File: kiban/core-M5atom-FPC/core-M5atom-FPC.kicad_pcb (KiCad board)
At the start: 2 copper layers, 49 x 40 mm, 18 parts, among them J12 TP_VIN, J13 TP_3V3, J14 TP_PGND, J15 TP_PGND, J16 ESP32-01, J17 ESP32-01, J18 TP_PGND, J3 M5atom-L, J4 M5atomS3-R, J5 3V3, J6 5V, J9 I2C, U1 AE-BNO055

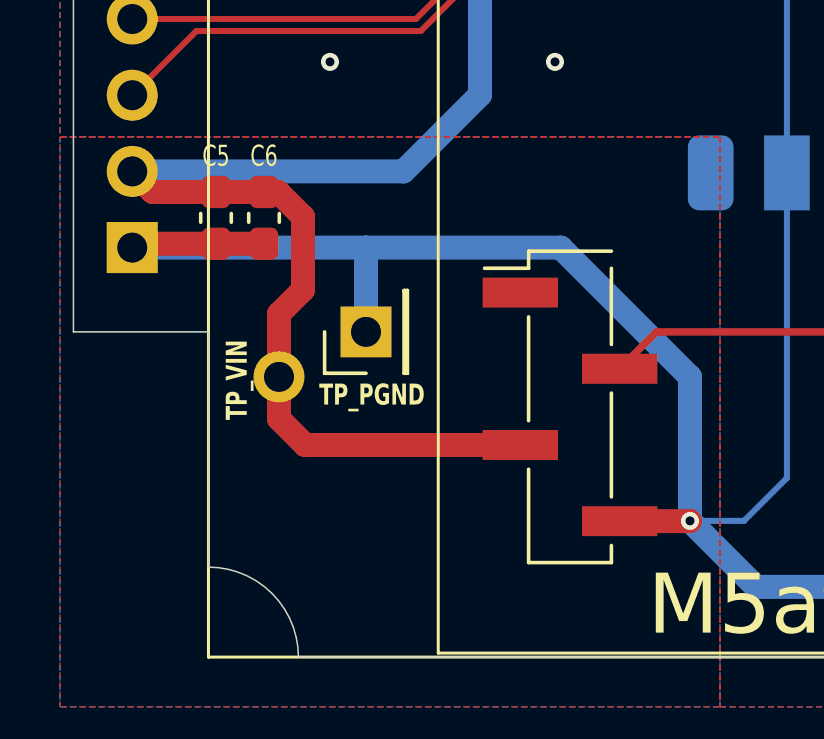
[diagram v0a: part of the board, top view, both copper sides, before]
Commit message: kiban: core-M5atom-FPC layout update + v02 iteration
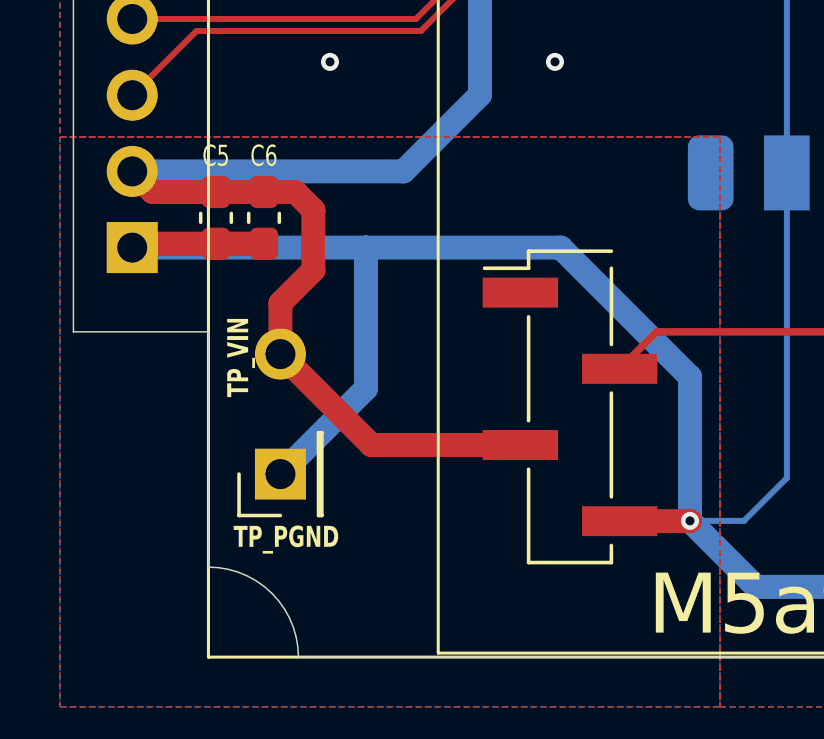
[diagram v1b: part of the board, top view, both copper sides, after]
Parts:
- moved J15 5.53 mm to (-17.6, 13.9)
- moved J12 0.76 mm to (-17.6, 9.90)
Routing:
- net GND: track 131.7 -> 137.6 mm
- net +5V: track 67.9 -> 67.2 mm
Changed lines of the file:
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@@
 	(footprint "Connector_PinHeader_2.54mm:PinHeader_1x01_P2.54mm_Vertical"
 		(layer "F.Cu")
-		(at -14.747867 9.1587 90)
+		(at -17.6 13.9 90)
 		(descr "Through hole straight pin header, 1x01, 2.54mm pitch, single row")
 		(tags "Through hole pin header THT 1x01 2.54mm single row")
@@
 	(footprint "Connector_PinHeader_2.54mm:PinHeader_1x01_P2.54mm_Vertical"
 		(layer "F.Cu")
-		(at -17.647867 10.6587)
+		(at -17.6 9.9)
 		(descr "Through hole straight pin header, 1x01, 2.54mm pitch, single row")
 		(tags "Through hole pin header THT 1x01 2.54mm single row")
@@
 	)
 	(segment
-		(start -17.447867 -13.8413)
-		(end -11.347867 -13.8413)
+		(start -17.1038 4.4962)
+		(end -18.147867 4.4962)
 		(width 0.8)
 		(layer "F.Cu")
@@
 	)
 	(segment
-		(start -10.947867 -13.4413)
-		(end -10.947867 -11.8413)
+		(start -16.5 7.1)
+		(end -16.5 5.1)
 		(width 0.8)
 		(layer "F.Cu")
@@
 	)
 	(segment
-		(start -18.147867 4.4962)
-		(end -19.747867 4.4962)
+		(start -16.5 5.1)
+		(end -17.1038 4.4962)
 		(width 0.8)
 		(layer "F.Cu")
@@
 	)
 	(segment
-		(start -17.672867 4.4962)
-		(end -18.147867 4.4962)
+		(start -17.447867 -13.8413)
+		(end -11.347867 -13.8413)
 		(width 0.8)
 		(layer "F.Cu")
@@
 	)
 	(segment
-		(start -21.853833 4.4962)
-		(end -22.54 3.810033)
+		(start -10.947867 -13.4413)
+		(end -10.947867 -11.8413)
 		(width 0.8)
 		(layer "F.Cu")
@@
 	)
 	(segment
-		(start -17.647867 8.5587)
-		(end -16.847867 7.7587)
+		(start -18.147867 4.4962)
+		(end -19.747867 4.4962)
 		(width 0.8)
 		(layer "F.Cu")
@@
 	(segment
 		(start -9.602867 12.9287)
-		(end -16.777867 12.9287)
-		(width 0.8)
-		(layer "F.Cu")
-		(net "+5V")
-	)
-	(segment
-		(start -16.847867 7.7587)
-		(end -16.847867 5.3212)
+		(end -14.5713 12.9287)
 		(width 0.8)
 		(layer "F.Cu")
@@
 	)
 	(segment
-		(start -17.647867 10.6587)
-		(end -17.647867 8.5587)
+		(start -21.853833 4.4962)
+		(end -22.54 3.810033)
 		(width 0.8)
 		(layer "F.Cu")
@@
 	)
 	(segment
-		(start -16.847867 5.3212)
-		(end -17.672867 4.4962)
+		(start -17.6 9.9)
+		(end -17.6 8.2)
 		(width 0.8)
 		(layer "F.Cu")
@@
 	)
 	(segment
-		(start -17.647867 12.0587)
-		(end -17.647867 10.6587)
+		(start -17.6 8.2)
+		(end -16.5 7.1)
 		(width 0.8)
 		(layer "F.Cu")
@@
 	)
 	(segment
-		(start -11.347867 -13.8413)
-		(end -10.947867 -13.4413)
+		(start -14.5713 12.9287)
+		(end -17.6 9.9)
 		(width 0.8)
 		(layer "F.Cu")
@@
 	)
 	(segment
-		(start -16.777867 12.9287)
-		(end -17.647867 12.0587)
+		(start -11.347867 -13.8413)
+		(end -10.947867 -13.4413)
 		(width 0.8)
 		(layer "F.Cu")
@@
 	)
 	(segment
+		(start -14.747867 11.047867)
+		(end -14.747867 6.350033)
+		(width 0.8)
+		(layer "B.Cu")
+		(net "GND")
+	)
+	(segment
 		(start -14.747867 6.350033)
 		(end -8.256534 6.350033)
@@
 	)
 	(segment
-		(start -14.747867 9.1587)
-		(end -14.747867 6.350033)
+		(start -17.6 13.9)
+		(end -14.747867 11.047867)
 		(width 0.8)
 		(layer "B.Cu")
